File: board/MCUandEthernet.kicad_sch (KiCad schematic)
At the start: 3 parts, among them J1 RJ45_LED_Shielded, U15 Teensy4.1_DEV-16771

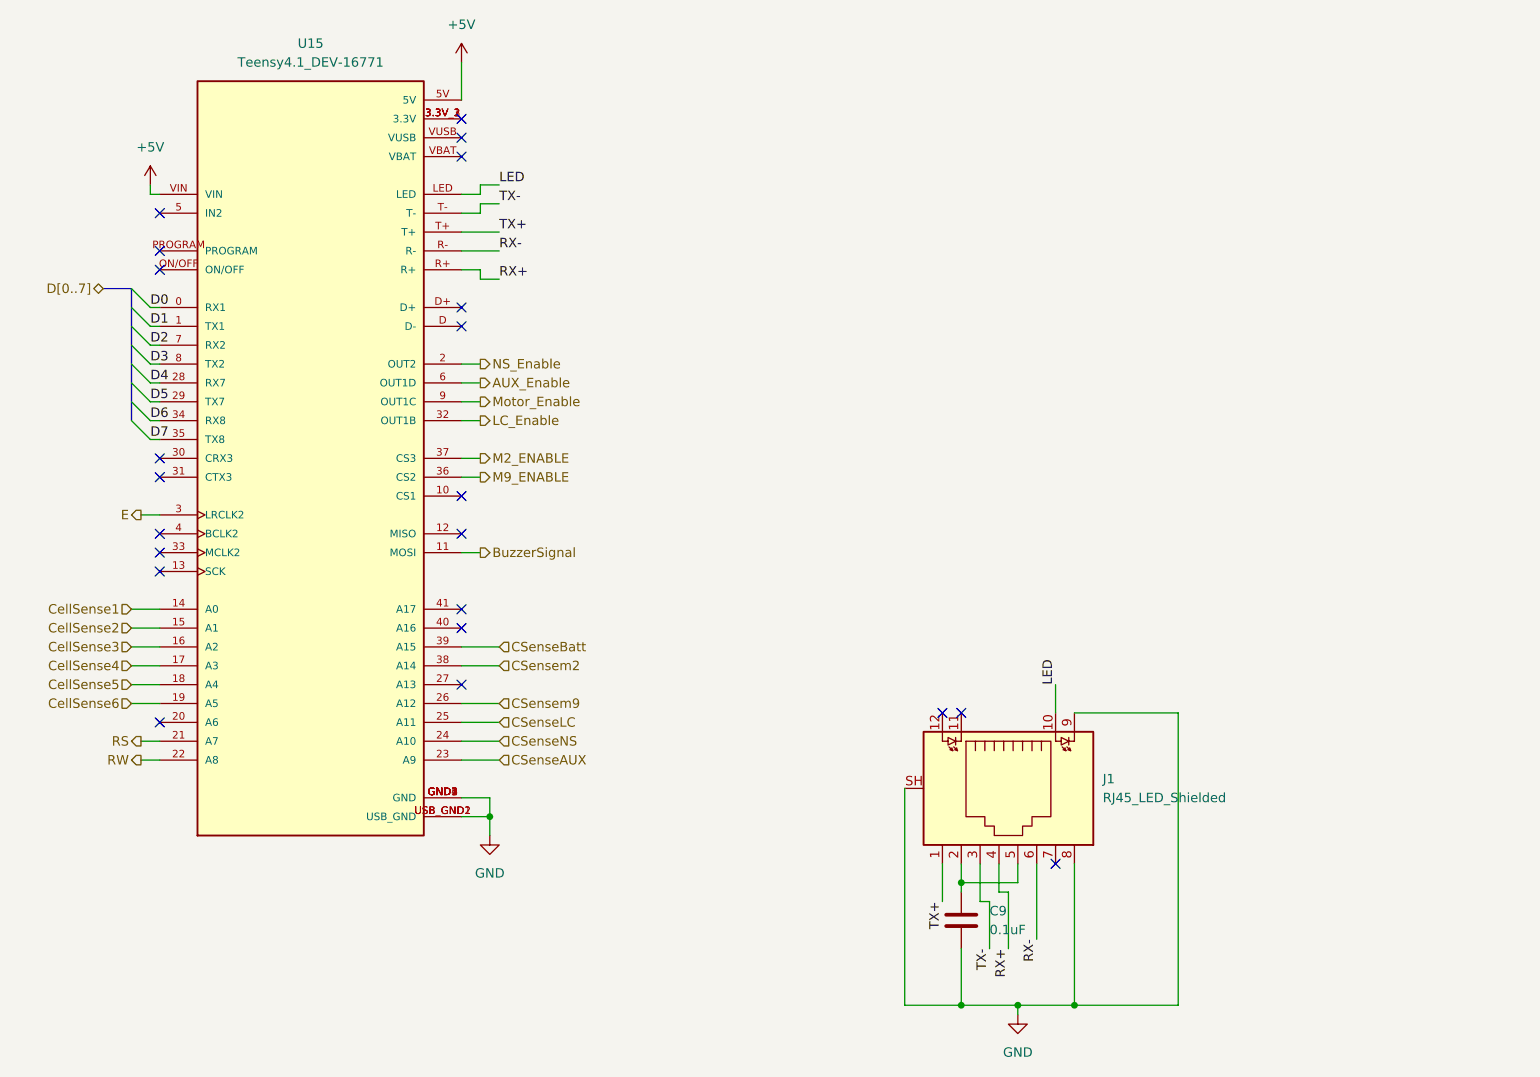
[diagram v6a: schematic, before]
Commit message: Center schematics and layout for prettiness
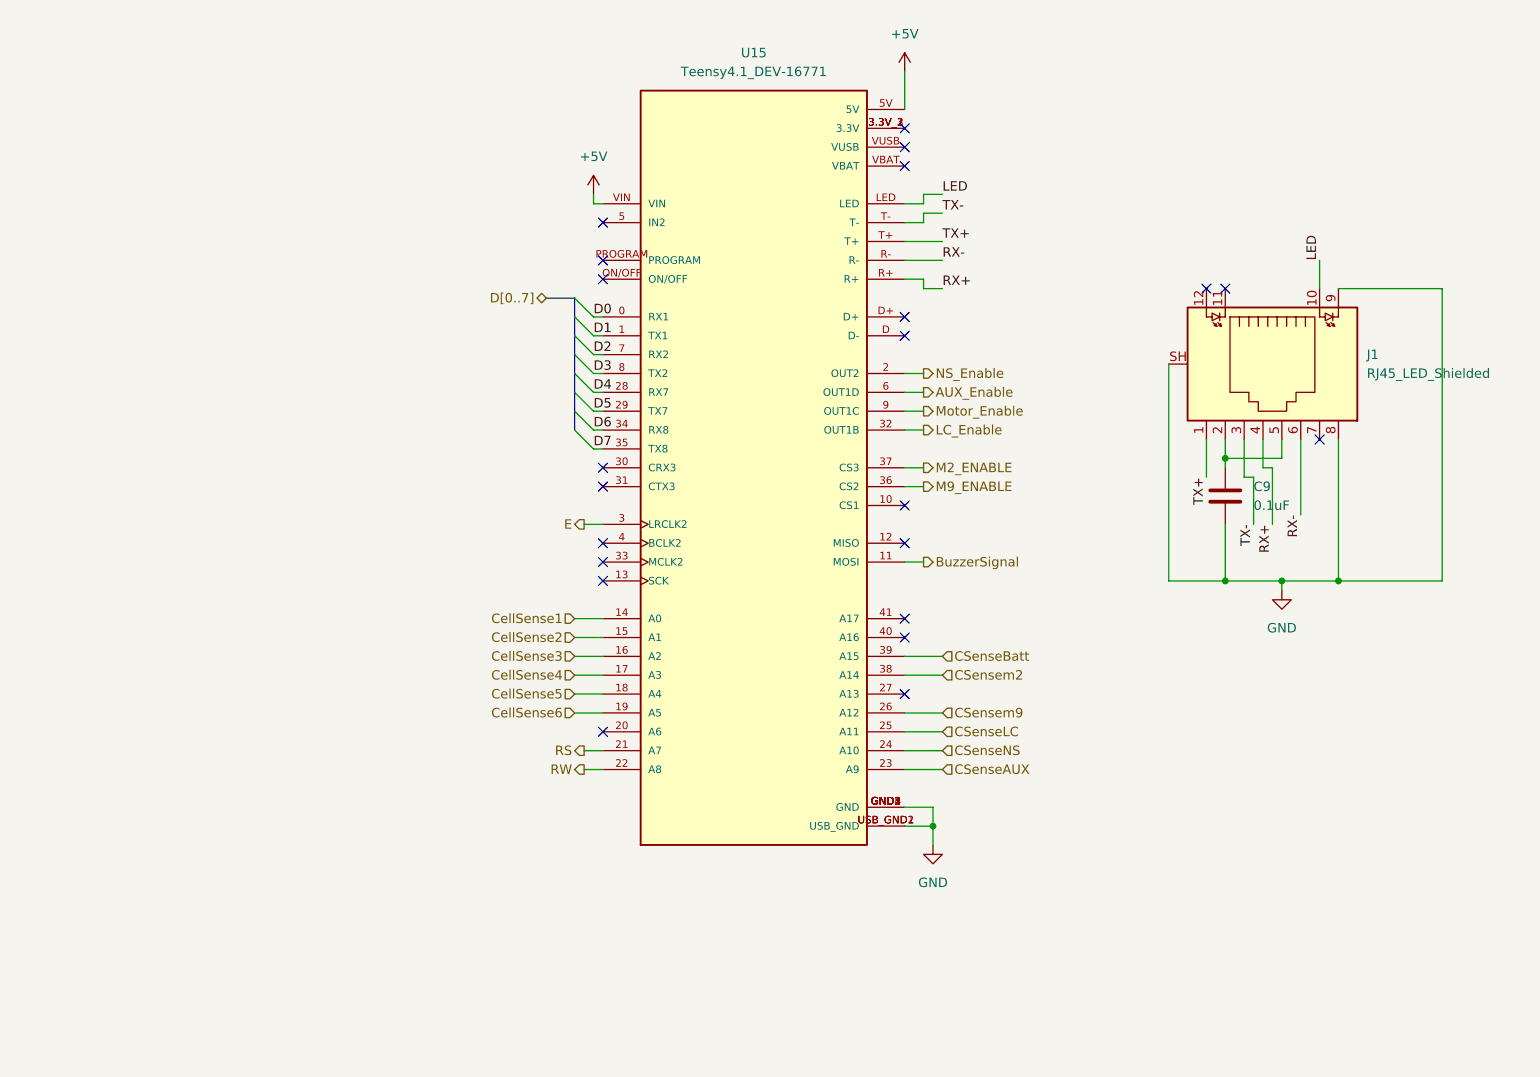
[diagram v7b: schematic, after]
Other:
- moved on the sheet: C9, J1, U15

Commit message: clean up board a tiny bit
this took way too long
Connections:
- net BuzzerSignal: now also U15.23 (A9); no longer U15.11 (MOSI)
- net CSenseAUX: now also U15.40 (A16); no longer U15.23 (A9)
- net CSenseBatt: now also U15.20 (A6); no longer U15.39 (A15)
- net CSenseLC: now also U15.19 (A5); no longer U15.25 (A11)
- net CSensem2: now also U15.27 (A13); no longer U15.38 (A14)
- net CellSense1: now also U15.41 (A17); no longer U15.14 (A0)
- net CellSense2: now also U15.14 (A0); no longer U15.15 (A1)
- net CellSense3: now also U15.15 (A1); no longer U15.16 (A2)
- net CellSense4: now also U15.16 (A2); no longer U15.17 (A3)
- net CellSense5: now also U15.17 (A3); no longer U15.18 (A4)
- net CellSense6: now also U15.18 (A4); no longer U15.19 (A5)
- net D0: now also U15.2 (OUT2); no longer U15.0 (RX1)
- net D2: now also U15.39 (A15); no longer U15.7 (RX2)
- net D3: now also U15.38 (A14); no longer U15.8 (TX2)
- net D4: now also U15.37 (CS3); no longer U15.28 (RX7)
- net D5: now also U15.36 (CS2); no longer U15.29 (TX7)
- net D6: now also U15.35 (TX8); no longer U15.34 (RX8)
- net D7: now also U15.34 (RX8); no longer U15.35 (TX8)
- net LC_Enable: now also U15.5 (IN2); no longer U15.32 (OUT1B)
- net M2_ENABLE: now also U15.28 (RX7); no longer U15.37 (CS3)
- net M9_ENABLE: now also U15.11 (MOSI); no longer U15.36 (CS2)
- net Motor_Enable: now also U15.4 (BCLK2); no longer U15.9 (OUT1C)
- net NS_Enable: now also U15.12 (MISO); no longer U15.2 (OUT2)
